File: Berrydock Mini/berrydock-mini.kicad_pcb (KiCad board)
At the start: 2 copper layers, 50 x 50 mm, 95 parts, among them J1 RJ45, P1 CONN_01X16, P2 CONN_01X16, P3 CONN_01X04, P4 CONN_01X03, P5 USB_OTG, P6 USB_A, SW1 SWITCH_INV, SW2 BUTTON, U1 USBLC6-2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

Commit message: First part of layout done
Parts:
- removed R22: 1K, Resistors_SMD:R_0603_HandSoldering
- P2: value CONN_01X16 -> CONN_01X11; footprint Pin_Headers:Pin_Header_Straight_1x16 -> Pin_Headers:Pin_Header_Straight_1x11
- moved C17 228.6 mm to (34.5, 97.9)
- moved C15 200.2 mm to (63.1, 97.6)
- moved C18 197.5 mm to (77.2, 100.6)
- moved U9 196.8 mm to (36.7, 95.4)
- moved C2 192.6 mm to (77.3, 69.6)
- moved C11 191.4 mm to (33.8, 95.3), turned to 90 degrees
- moved R23 186.5 mm to (36.7, 92.8)
- moved R25 185.1 mm to (59.3, 97.6)
- moved R21 183.7 mm to (33.7, 91.7), turned to 270 degrees
- moved P4 179.3 mm to (60.4, 101.0)
- moved U14 175.4 mm to (74.5, 25.8)
- moved R11 175.0 mm to (82.1, 48.9)
- moved U4 174.5 mm to (62.2, 47.9), turned to 180 degrees
- moved J1 169.2 mm to (60.2, 60.0)
- moved D1 167.1 mm to (105.3, 110.2), turned to 180 degrees
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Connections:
- P2 pad 10: /ETH_TX+ -> /GPIO5
- P2 pad 11: /ETH_RX- -> +5V
- P2 pad 3: /UH_+ -> /RX0
- P2 pad 4: /UH_- -> /TX0
- P2 pad 5: /RX0 -> /FW_RST
- P2 pad 6: /TX0 -> +3.3VP
- P2 pad 7: /FW_RST -> /GPIO18
- P2 pad 8: +3.3VP -> /GPIO19
- P2 pad 9: /ETH_TX- -> /GPIO4
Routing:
- added copper zone on B.Cu, net GND
- added copper zone on F.Cu, net GND

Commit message: laid everything out
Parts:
- removed C2, C3: 100nF, Capacitors_SMD:C_0603
- removed JP1, JP2: Jumper_NO_Small, Pin_Headers:Pin_Header_Straight_1x02
- removed R2: 2K, Resistors_SMD:R_0603_HandSoldering
- removed R3: 3K, Resistors_SMD:R_0603_HandSoldering
- removed U1, U2: USBLC6-2, Omega2-Berrydock:SOT32-6L
- removed U6, U7: SMP75, Omega2-Berrydock:DO-214AA
- R11, R12, R6, R7, R8, R9: footprint Resistors_SMD:R_0603_HandSoldering -> Resistors_SMD:R_0603
- moved C12 117.0 mm to (27.8, 60.0)
- moved C16 113.7 mm to (36.0, 56.8)
- moved L3 113.7 mm to (33.5, 51.9)
- moved R24 113.7 mm to (34.0, 56.8)
- moved R14 113.7 mm to (35.3, 59.8)
- moved U10 113.7 mm to (31.3, 57.7)
- moved R17 113.6 mm to (26.9, 57.1)
- moved R15 113.6 mm to (28.7, 57.1)
- moved SW2 110.1 mm to (33.5, 69.0), turned to 180 degrees
- moved F1 108.1 mm to (54.8, 39.1), turned to 270 degrees
- moved R26 106.6 mm to (45.5, 42.5), turned to 0 degrees
- moved R27 103.4 mm to (46.4, 46.4), turned to 270 degrees
- moved P3 100.0 mm to (58.3, 40.9), turned to 180 degrees
- moved SW1 99.2 mm to (24.6, 68.0), turned to 180 degrees
- moved R10 94.1 mm to (22.3, 64.2), turned to 180 degrees
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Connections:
- C23 pad 2: +5VD -> +5V
- R6 pad 1: Net-(R6-Pad1) -> /ETH_TX+
- R8 pad 1: Net-(R8-Pad1) -> /ETH_TX-
- R9 pad 2: Net-(R9-Pad2) -> /ETH_RX+
- SW2 pad 1: Net-(R27-Pad2) -> +3V3
- SW2 pad 2: +3V3 -> Net-(R27-Pad2)
- U4 pad 1: Net-(R6-Pad1) -> /ETH_TX+
- U4 pad 3: Net-(R8-Pad1) -> /ETH_TX-
- U4 pad 6: Net-(R9-Pad2) -> /ETH_RX+

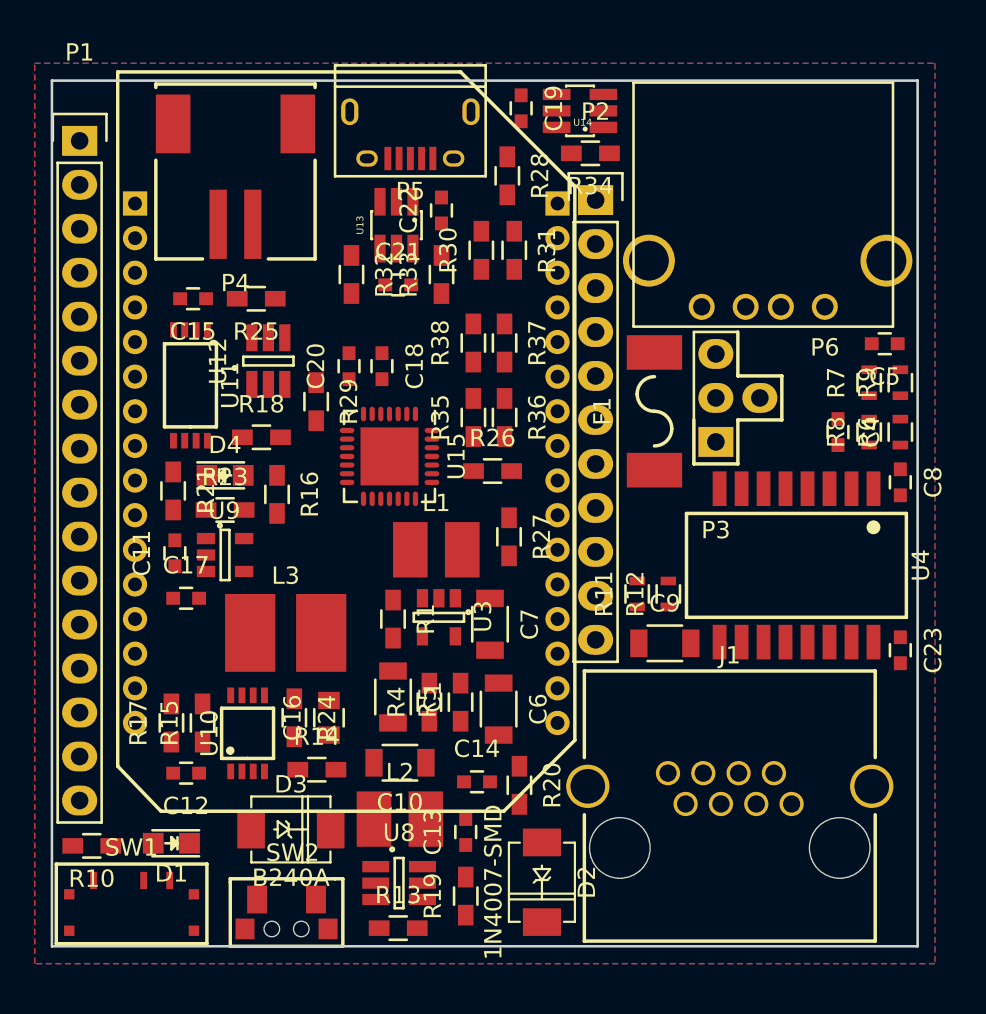
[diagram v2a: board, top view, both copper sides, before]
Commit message: Finished Routing, only BoM and some nice graphics left to do
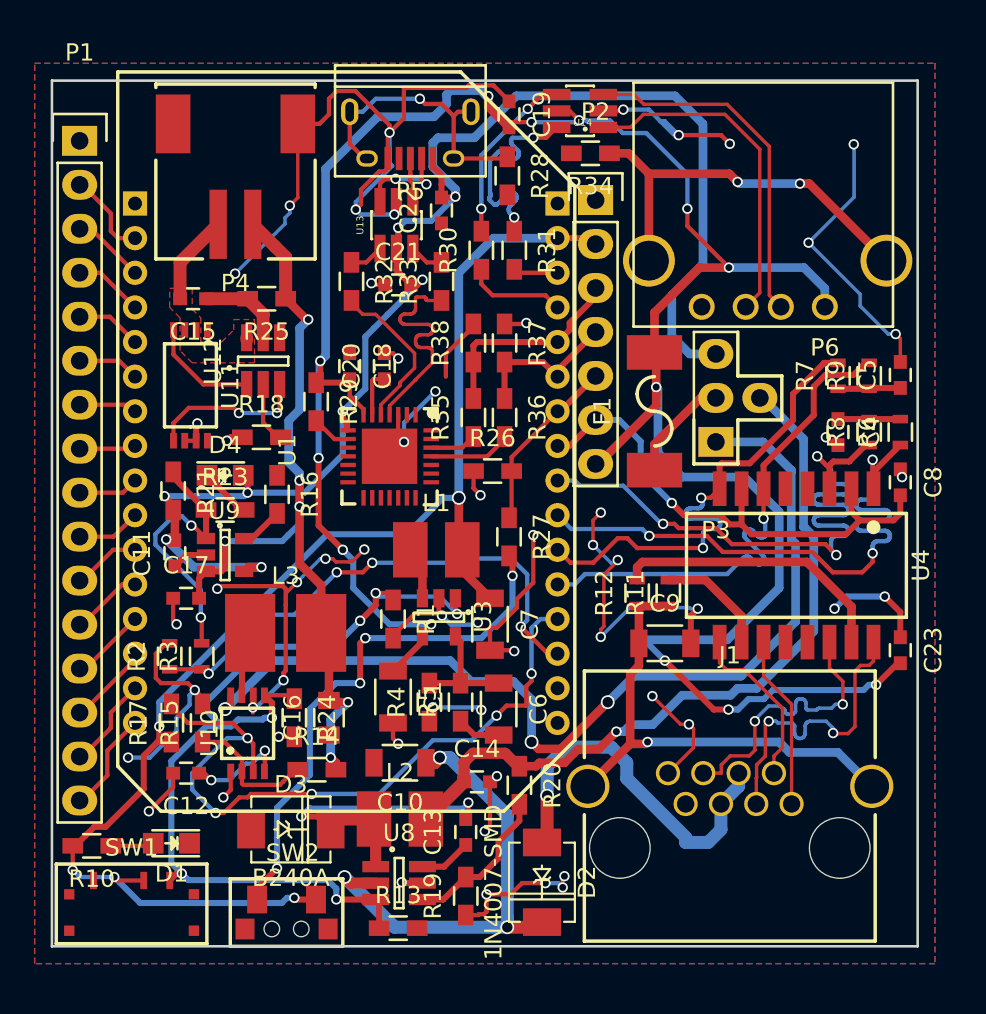
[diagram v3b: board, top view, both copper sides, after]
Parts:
- removed U15: CP2102, Housings_DFN_QFN:QFN-28-1EP_5x5mm_Pitch0.5mm
- added R2: 3K, Resistors_SMD:R_0603, F.Cu at (26.8, 53.2)
- added R3: 2K, Resistors_SMD:R_0603, F.Cu at (28.6, 53.2)
- added U1: CP2102, Omega2-Berrydock:QFN-28, F.Cu at (39.5, 41.7)
- P2: value CONN_01X11 -> CONN_01X07; footprint Pin_Headers:Pin_Header_Straight_1x11 -> Pin_Headers:Pin_Header_Straight_1x07
- moved C20 2.04 mm to (39.2, 36.5)
- moved C5 2.01 mm to (69.0, 37.0), turned to 90 degrees
- moved C18 1.86 mm to (37.2, 36.5)
- moved R7 1.84 mm to (65.4, 37.0)
- moved R9 1.84 mm to (67.2, 37.0)
- moved R11 1.80 mm to (55.6, 49.6)
- moved R12 1.80 mm to (53.8, 49.6)
- moved C19 0.78 mm to (46.4, 21.9)
- moved R25 0.60 mm to (32.4, 32.6)
- moved R32 0.40 mm to (37.3, 31.6)
- moved R33 0.40 mm to (42.5, 31.6)
- moved U12 0.30 mm to (32.2, 36.2)
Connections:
- net Net-(J1-Pad1) renamed /RX_R_P
- net Net-(J1-Pad2) renamed /RX_R_N
- net Net-(J1-Pad3) renamed /TX_R_P
- net Net-(J1-Pad6) renamed /TX_R_N
- P2 pad 7: /GPIO18 -> +5V
- P3 pad 2: +5VD -> +5P
- P3 pad 3: +5P -> +5VD
- R7 pad 2: Net-(R7-Pad2) -> /ETH_RX-
- U4 pad 8: Net-(R7-Pad2) -> /ETH_RX-
- U5 pad 17: /GPIO5 -> Net-(U5-Pad17)
- U5 pad 18: /GPIO4 -> Net-(U5-Pad18)
- U5 pad 19: /GPIO19 -> Net-(R2-Pad1)
- U5 pad 20: /GPIO18 -> /LBO
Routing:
- net GND: track 0.00 -> 188.8 mm, vias 0 -> 56
- net +5V: track 0.00 -> 139.4 mm, vias 0 -> 13
- net +5VD: track 0.00 -> 85.0 mm, vias 0 -> 8
- net +3V3: track 0.00 -> 80.4 mm, vias 0 -> 5
- net +5VP: track 0.00 -> 55.5 mm, vias 0 -> 3
- net /PWRON: track 0.00 -> 53.7 mm, vias 0 -> 6
- net VPP: track 0.00 -> 46.0 mm, vias 0 -> 6
- net +5P: track 0.00 -> 43.1 mm, vias 0 -> 1
- net /LBO: track 0.00 -> 41.2 mm, vias 0 -> 5
- net /ETH_TX-: track 0.00 -> 37.5 mm, vias 0 -> 3
- net /ETH_TX+: track 0.00 -> 36.1 mm, vias 0 -> 3
- net Net-(R27-Pad2): track 0.00 -> 30.8 mm, vias 0 -> 4
- net /ETH_RX+: track 0.00 -> 30.0 mm, vias 0 -> 1
- net Net-(R2-Pad1): track 0.00 -> 29.8 mm, vias 0 -> 4
- net +3.3VP: track 0.00 -> 29.8 mm, vias 0 -> 1
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- added copper zone on F.Cu, net /BAT_-
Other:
- net class Default: trace_width 0.25 -> 0.2

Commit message: Finished BOM Cost
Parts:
- C6: footprint Capacitors_SMD:C_1206 -> Capacitors_SMD:C_0603
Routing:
- net GND: track 188.8 -> 191.5 mm, vias 56 -> 57
- net Net-(P6-Pad5): track 23.6 -> 24.1 mm
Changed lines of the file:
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@@
     (thickness 1.6)
     (drawings 4)
-    (tracks 1599)
+    (tracks 1611)
     (zones 0)
     (modules 86)
@@
   )
   (setup
-    (last_trace_width 0.2)
+    (last_trace_width 0.5)
     (user_trace_width 0.25)
     (user_trace_width 0.35)
@@
   )
   (module Capacitors_SMD:C_1206 (layer F.Cu)
-    (at 45.8 56.3 270)
-    (descr "Capacitor SMD 1206, reflow soldering, AVX (see smccp.pdf)")
-    (tags "capacitor 1206")
-    (attr smd)
-    (fp_text reference C6 (at 0 -2.3 270) (layer F.SilkS)
-      (effects (font (size 1 1) (thickness 0.15)))
-    )
-    (fp_text value 22nF (at 0 2.3 270) (layer F.Fab)
-      (effects (font (size 1 1) (thickness 0.15)))
-    )
-    (fp_line (start -2.3 -1.15) (end 2.3 -1.15) (layer F.CrtYd) (width 0.05))
-    (fp_line (start -2.3 1.15) (end 2.3 1.15) (layer F.CrtYd) (width 0.05))
-    (fp_line (start -2.3 -1.15) (end -2.3 1.15) (layer F.CrtYd) (width 0.05))
-    (fp_line (start 2.3 -1.15) (end 2.3 1.15) (layer F.CrtYd) (width 0.05))
-    (fp_line (start 1 -1.025) (end -1 -1.025) (layer F.SilkS) (width 0.15))
-    (fp_line (start -1 1.025) (end 1 1.025) (layer F.SilkS) (width 0.15))
-    (pad 1 smd rect (at -1.5 0 270) (size 1 1.6) (layers F.Cu F.Paste F.Mask)
-      (net 6 "Net-(C6-Pad1)"))
-    (pad 2 smd rect (at 1.5 0 270) (size 1 1.6) (layers F.Cu F.Paste F.Mask)
-      (net 7 "Net-(C6-Pad2)"))
-    (model Capacitors_SMD.3dshapes/C_1206.wrl
-      (at (xyz 0 0 0))
-      (scale (xyz 1 1 1))
-      (rotate (xyz 0 0 0))
-    )
-  )
-  (module Capacitors_SMD:C_1206 (layer F.Cu)
     (at 45.3 51.4 270)
     (descr "Capacitor SMD 1206, reflow soldering, AVX (see smccp.pdf)")
@@
       (net 2 GND))
   )
+  (module Capacitors_SMD:C_0603 (layer F.Cu)
+    (at 45.8 56.3 270)
+    (descr "Capacitor SMD 0603, reflow soldering, AVX (see smccp.pdf)")
+    (tags "capacitor 0603")
+    (attr smd)
+    (fp_text reference C6 (at 0 -1.9 270) (layer F.SilkS)
+      (effects (font (size 1 1) (thickness 0.15)))
+    )
+    (fp_text value 22nF (at 0 1.9 270) (layer F.Fab)
+      (effects (font (size 1 1) (thickness 0.15)))
+    )
+    (fp_line (start -1.45 -0.75) (end 1.45 -0.75) (layer F.CrtYd) (width 0.05))
+    (fp_line (start -1.45 0.75) (end 1.45 0.75) (layer F.CrtYd) (width 0.05))
+    (fp_line (start -1.45 -0.75) (end -1.45 0.75) (layer F.CrtYd) (width 0.05))
+    (fp_line (start 1.45 -0.75) (end 1.45 0.75) (layer F.CrtYd) (width 0.05))
+    (fp_line (start -0.35 -0.6) (end 0.35 -0.6) (layer F.SilkS) (width 0.15))
+    (fp_line (start 0.35 0.6) (end -0.35 0.6) (layer F.SilkS) (width 0.15))
+    (pad 1 smd rect (at -0.75 0 270) (size 0.8 0.75) (layers F.Cu F.Paste F.Mask)
+      (net 6 "Net-(C6-Pad1)"))
+    (pad 2 smd rect (at 0.75 0 270) (size 0.8 0.75) (layers F.Cu F.Paste F.Mask)
+      (net 7 "Net-(C6-Pad2)"))
+    (model Capacitors_SMD.3dshapes/C_0603.wrl
+      (at (xyz 0 0 0))
+      (scale (xyz 1 1 1))
+      (rotate (xyz 0 0 0))
+    )
+  )
   (gr_line (start 20 70) (end 20 20) (angle 90) (layer Edge.Cuts) (width 0.15))
   (gr_line (start 70 70) (end 20 70) (angle 90) (layer Edge.Cuts) (width 0.15))
@@
   (segment (start 37.996198 39.255992) (end 37.996198 38.980992) (width 0.25) (layer F.Cu) (net 1))
   (segment (start 37.996198 38.980992) (end 37.2 38.184794) (width 0.25) (layer F.Cu) (net 1))
+  (segment (start 56.2 23.15) (end 55.14 23.15) (width 0.5) (layer F.Cu) (net 2))
+  (segment (start 55.14 23.15) (end 53.96 24.33) (width 0.5) (layer F.Cu) (net 2))
+  (via (at 53.96 24.33) (size 0.6) (drill 0.4) (layers F.Cu B.Cu) (net 2))
   (segment (start 37.229998 47.75) (end 37.37 47.75) (width 0.2) (layer F.Cu) (net 2))
   (via (at 38.04 47.08) (size 0.6) (drill 0.4) (layers F.Cu B.Cu) (net 2))
@@
   (segment (start 67.25 37.75) (end 67.2 37.8) (width 0.35) (layer F.Cu) (net 5))
   (segment (start 65.4 37.8) (end 67.2 37.8) (width 0.35) (layer F.Cu) (net 5))
+  (segment (start 44.99 54.8) (end 43.6 54.8) (width 0.35) (layer F.Cu) (net 6))
+  (segment (start 45.8 55.525) (end 45.075 54.8) (width 0.35) (layer F.Cu) (net 6))
+  (segment (start 45.8 55.55) (end 45.8 55.525) (width 0.35) (layer F.Cu) (net 6))
+  (segment (start 45.075 54.8) (end 44.99 54.8) (width 0.35) (layer F.Cu) (net 6))
   (segment (start 43.6 54.8) (end 43.6 52.4) (width 0.35) (layer F.Cu) (net 6))
   (segment (start 43.6 52.4) (end 43.3 52.1) (width 0.35) (layer F.Cu) (net 6))
   (segment (start 43.6 54.8) (end 41.8 54.8) (width 0.35) (layer F.Cu) (net 6))
-  (segment (start 45.8 54.8) (end 43.6 54.8) (width 0.35) (layer F.Cu) (net 6))
-  (segment (start 45.8 57.8) (end 44.4 57.8) (width 0.35) (layer F.Cu) (net 7))
+  (segment (start 44.4 57.8) (end 45.075 57.8) (width 0.35) (layer F.Cu) (net 7))
+  (segment (start 45.075 57.8) (end 45.8 57.075) (width 0.35) (layer F.Cu) (net 7))
+  (segment (start 45.8 57.075) (end 45.8 57.05) (width 0.35) (layer F.Cu) (net 7))
+  (segment (start 43.6 57) (end 43.65 57.05) (width 0.35) (layer F.Cu) (net 7))
   (segment (start 44.4 57.8) (end 43.6 57) (width 0.35) (layer F.Cu) (net 7))
   (segment (start 26.2 57.3) (end 26.2 58.1) (width 0.35) (layer F.Cu) (net 8))
@@
   (segment (start 54.8 41) (end 57.472 38.328) (width 0.5) (layer F.Cu) (net 23))
   (segment (start 57.472 38.328) (end 58.346 38.328) (width 0.5) (layer F.Cu) (net 23))
+  (segment (start 47.4 54.974264) (end 47.4 55.71) (width 0.25) (layer F.Cu) (net 24))
+  (segment (start 46.93 56.85) (end 46.93 56.425736) (width 0.25) (layer F.Cu) (net 24))
+  (segment (start 46.93 56.425736) (end 47.4 55.955736) (width 0.25) (layer F.Cu) (net 24))
+  (segment (start 47.4 55.955736) (end 47.4 55.71) (width 0.25) (layer F.Cu) (net 24))
+  (segment (start 45.680515 56.675491) (end 46.755491 56.675491) (width 0.25) (layer B.Cu) (net 24))
+  (segment (start 46.755491 56.675491) (end 46.93 56.85) (width 0.25) (layer B.Cu) (net 24))
+  (via (at 46.93 56.85) (size 0.6) (drill 0.4) (layers F.Cu B.Cu) (net 24))
   (segment (start 31.3 57.975) (end 30.125 57.975) (width 0.25) (layer B.Cu) (net 24))
   (segment (start 30.125 57.975) (end 28.1 60) (width 0.25) (layer B.Cu) (net 24))
@@
   (segment (start 47.7 54.25) (end 47.7 54.674264) (width 0.25) (layer F.Cu) (net 24))
   (segment (start 47.7 54.674264) (end 47.4 54.974264) (width 0.25) (layer F.Cu) (net 24))
-  (segment (start 47.4 54.974264) (end 47.4 56.1) (width 0.25) (layer F.Cu) (net 24))
   (segment (start 47.7 51.610051) (end 47.7 54.25) (width 0.25) (layer B.Cu) (net 24))
   (via (at 47.7 54.25) (size 0.6) (drill 0.4) (layers F.Cu B.Cu) (net 24))
-  (via (at 45.680515 56.675491) (size 0.6) (drill 0.4) (layers F.Cu B.Cu) (net 24))
-  (segment (start 45.809511 56.675491) (end 45.680515 56.675491) (width 0.25) (layer F.Cu) (net 24))
-  (segment (start 46.256006 56.1) (end 45.680515 56.675491) (width 0.25) (layer F.Cu) (net 24))
-  (segment (start 47.4 56.1) (end 46.256006 56.1) (width 0.25) (layer F.Cu) (net 24))
   (segment (start 49.2 51.1) (end 48.210051 51.1) (width 0.25) (layer B.Cu) (net 24))
   (segment (start 48.210051 51.1) (end 47.7 51.610051) (width 0.25) (layer B.Cu) (net 24))
@@
   (segment (start 61.433 23.803) (end 61.433 32.4) (width 0.2) (layer F.Cu) (net 57))
   (segment (start 61.433 32.4) (end 62.1 33.067) (width 0.2) (layer F.Cu) (net 57))
+  (segment (start 52.2 24.2) (end 52.2 25.15) (width 0.5) (layer F.Cu) (net 58))
+  (segment (start 52.2 25.15) (end 52.43 25.38) (width 0.5) (layer F.Cu) (net 58))
+  (segment (start 52.43 25.38) (end 54.48 25.38) (width 0.5) (layer F.Cu) (net 58))
   (segment (start 54.48 25.38) (end 54.48 30.4) (width 0.5) (layer F.Cu) (net 58))
-  (segment (start 53.3 24.2) (end 54.48 25.38) (width 0.5) (layer F.Cu) (net 58))
-  (segment (start 52.2 24.2) (end 53.3 24.2) (width 0.5) (layer F.Cu) (net 58))
   (segment (start 59.6 25.85) (end 59.13 25.38) (width 0.5) (layer F.Cu) (net 58))
   (segment (start 59.13 25.38) (end 54.48 25.38) (width 0.5) (layer F.Cu) (net 58))
